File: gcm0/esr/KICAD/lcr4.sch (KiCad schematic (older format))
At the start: 107 parts, among them J1 Conn_Coaxial, J2 Conn_Coaxial, J3 Conn_Coaxial, J4 Conn_Coaxial, SW1 SW_Push, SW2 SW_Push, U1 NE5532, U2 CD4053B, U3 TL084, U4 LM7805_TO220, U5 LM2596S-5, U6 LM1117-3.3, U7 74HC595, U8 STM32F030F4P6, Y1 8M

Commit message: esr电路改错
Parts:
- removed J1, J2, J3, J4: Conn_Coaxial, symbol Connector:Conn_Coaxial
- added D15, D16: 1N4007, Diode_THT:D_DO-41_SOD81_P10.16mm_Horizontal, symbol Diode:1N4007
- added J1, J2, J3, J4: Conn_01x01_Male, Connector_PinHeader_2.54mm:PinHeader_1x01_P2.54mm_Vertical, symbol Connector:Conn_01x01_Male
- added K1, K2: DIPxx-1Axx-11x, Relay_THT:Relay_SPDT_Finder_36.11, symbol Relay:DIPxx-1Axx-11x
- added Q1, Q2: BC547, Package_TO_SOT_THT:TO-92_Inline, symbol Transistor_BJT:BC547
- added R39: 100, Resistor_THT:R_Axial_DIN0204_L3.6mm_D1.6mm_P2.54mm_Vertical, symbol Device:R
- added R40: 1, Resistor_THT:R_Axial_DIN0204_L3.6mm_D1.6mm_P2.54mm_Vertical, symbol Device:R
- added R41, R42: R, Resistor_THT:R_Axial_DIN0204_L3.6mm_D1.6mm_P2.54mm_Vertical, symbol Device:R
- C1, C2, C4: footprint (none) -> Capacitor_THT:C_Rect_L11.0mm_W4.2mm_P10.00mm_MKT
- C10, C11, C12, C13, C14, C15, C16, C17, C18, C19, C20, C21, C22, C23, C24, C25, C26, C27, C28, C29, C3, C31, C32, C33, C34, C35, C36, C37, C5, C6, C7, C8, C9: footprint (none) -> Capacitor_SMD:C_0805_2012Metric_Pad1.18x1.45mm_HandSolder
- C30: value C -> 104; footprint (none) -> Capacitor_SMD:C_0805_2012Metric_Pad1.18x1.45mm_HandSolder
- L1: footprint (none) -> Inductor_THT:L_Radial_D8.7mm_P5.00mm_Fastron_07HCP
- R1: value 100 -> 10K; footprint (none) -> Resistor_THT:R_Axial_DIN0204_L3.6mm_D1.6mm_P2.54mm_Vertical
- R10, R11, R12, R13, R14, R15, R16, R17, R18, R19, R2, R20, R21, R22, R23, R24, R25, R26, R3, R32, R33, R34, R35, R36, R37, R38, R4, R5, R6, R7, R8, R9: footprint (none) -> Resistor_THT:R_Axial_DIN0204_L3.6mm_D1.6mm_P2.54mm_Vertical
- R27, R28, R29: value R -> 10K; footprint (none) -> Resistor_THT:R_Axial_DIN0204_L3.6mm_D1.6mm_P2.54mm_Vertical
- R30: value R -> 1.5K; footprint (none) -> Resistor_THT:R_Axial_DIN0204_L3.6mm_D1.6mm_P2.54mm_Vertical
- R31: value R -> 1K; footprint (none) -> Resistor_THT:R_Axial_DIN0204_L3.6mm_D1.6mm_P2.54mm_Vertical
- SW1, SW2: footprint (none) -> Button_Switch_THT:SW_Tactile_SPST_Angled_PTS645Vx83-2LFS
- TR1: footprint (none) -> Transformer_THT:Transformer_Toroid_Horizontal_D10.5mm_Amidon-T37
- U1: footprint (none) -> Package_DIP:DIP-8_W7.62mm
- U2, U7: footprint (none) -> Package_DIP:DIP-16_W7.62mm
- U3: footprint (none) -> Package_DIP:DIP-14_W7.62mm
- U6: footprint (none) -> Package_TO_SOT_SMD:SOT-223-3_TabPin2
- Y1: footprint (none) -> Crystal:Crystal_HC49-U_Vertical
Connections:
- net +5V: now also D15.1 (K), D16.1 (K), K1.7, K1.8, K2.7, K2.8
- net GND: now also Q1.3 (E), Q2.3 (E)
- net at R3.2: now also J3.1 (Pin_1)
- net at TR1.1: now also J4.1 (Pin_1)
- net at R1.2: now also J1.1 (Pin_1), K1.2, K2.2
- net at R2.2: now also J2.1 (Pin_1)
- net at R1.1, R9.2, TR1.2: now also R39.1, R40.1
- net PA6_1_R: now reaches U8.12 (PA6)
- net PA6_1_R: now also R41.1
- net PA9_100_R: now reaches U8.17 (PA9)
- net PA9_100_R: now also R42.1
- new net: D15.2 (A), K1.1, K1.14, Q1.1 (C)
- new net: K1.6, R39.2
- new net: D16.2 (A), K2.1, K2.14, Q2.1 (C)
- new net: K2.6, R40.2
- new net: Q1.2 (B), R42.2
- new net: Q2.2 (B), R41.2
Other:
- moved on the sheet: C1, D3, D6, R2, R5

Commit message: 修改电路
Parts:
- R41: value R -> 1K
- R42: value R -> 1k
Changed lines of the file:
@@
 P 4400 5350
 F 0 "R41" V 4193 5350 50  0000 C CNN
-F 1 "R" V 4284 5350 50  0000 C CNN
+F 1 "1K" V 4284 5350 50  0000 C CNN
 F 2 "Resistor_THT:R_Axial_DIN0204_L3.6mm_D1.6mm_P2.54mm_Vertical" V 4330 5350 50  0001 C CNN
 F 3 "~" H 4400 5350 50  0001 C CNN
@@
 P 4400 5650
 F 0 "R42" V 4193 5650 50  0000 C CNN
-F 1 "R" V 4284 5650 50  0000 C CNN
+F 1 "1k" V 4284 5650 50  0000 C CNN
 F 2 "Resistor_THT:R_Axial_DIN0204_L3.6mm_D1.6mm_P2.54mm_Vertical" V 4330 5650 50  0001 C CNN
 F 3 "~" H 4400 5650 50  0001 C CNN

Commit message: ..
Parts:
- removed D15, D16: 1N4007, Diode_THT:D_DO-41_SOD81_P10.16mm_Horizontal, symbol Diode:1N4007
- removed K1, K2: DIPxx-1Axx-11x, Relay_THT:Relay_SPDT_Finder_36.11, symbol Relay:DIPxx-1Axx-11x
- removed Q1, Q2: BC547, Package_TO_SOT_THT:TO-92_Inline, symbol Transistor_BJT:BC547
- removed R1: 10K, Resistor_THT:R_Axial_DIN0204_L3.6mm_D1.6mm_P2.54mm_Vertical, symbol Device:R
- removed R39: 100, Resistor_THT:R_Axial_DIN0204_L3.6mm_D1.6mm_P2.54mm_Vertical, symbol Device:R
- removed R40: 1, Resistor_THT:R_Axial_DIN0204_L3.6mm_D1.6mm_P2.54mm_Vertical, symbol Device:R
- removed R41: 1K, Resistor_THT:R_Axial_DIN0204_L3.6mm_D1.6mm_P2.54mm_Vertical, symbol Device:R
- removed R42: 1k, Resistor_THT:R_Axial_DIN0204_L3.6mm_D1.6mm_P2.54mm_Vertical, symbol Device:R
- added R?: 100, symbol Device:R
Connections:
- net at R9.2, TR1.2: now also R?.1
- net at J1.1 (Pin_1): now also R?.2
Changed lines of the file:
@@
 	2050 2600 1650 2600
-$Comp
-L Device:R R1
-U 1 1 62031458
-P 1700 4350
-F 0 "R1" H 1770 4396 50  0000 L CNN
-F 1 "10K" H 1770 4305 50  0000 L CNN
-F 2 "Resistor_THT:R_Axial_DIN0204_L3.6mm_D1.6mm_P2.54mm_Vertical" V 1630 4350 50  0001 C CNN
-F 3 "~" H 1700 4350 50  0001 C CNN
-	1    1700 4350
-	1    0    0    -1
-$EndComp
 $Comp
 L Device:C C3
@@
 	1650 5800 1600 5800
 Wire Wire Line
-	1600 5150 1700 5150
-Wire Wire Line
-	1700 4200 1700 4100
-Wire Wire Line
 	1700 3600 2050 3600
-Wire Wire Line
-	1700 4500 1700 5150
 Wire Wire Line
 	3700 4250 3800 4250
@@
 	9050 3900 9050 4000
 Connection ~ 9050 4000
-$Comp
-L Relay:DIPxx-1Axx-11x K1
-U 1 1 620DB42C
-P 2250 4850
-F 0 "K1" H 2200 4550 50  0000 L CNN
-F 1 "DIPxx-1Axx-11x" H 1700 4400 50  0000 L CNN
-F 2 "Relay_THT:Relay_SPDT_Finder_36.11" H 2600 4800 50  0001 L CNN
-F 3 "https://standexelectronics.com/wp-content/uploads/datasheet_reed_relay_DIP.pdf" H 2250 4850 50  0001 C CNN
-	1    2250 4850
-	1    0    0    -1
-$EndComp
-$Comp
-L Relay:DIPxx-1Axx-11x K2
-U 1 1 620DE9A0
-P 3450 4850
-F 0 "K2" H 3400 5150 50  0000 L CNN
-F 1 "DIPxx-1Axx-11x" H 2950 4500 50  0000 L CNN
-F 2 "Relay_THT:Relay_SPDT_Finder_36.11" H 3800 4800 50  0001 L CNN
-F 3 "https://standexelectronics.com/wp-content/uploads/datasheet_reed_relay_DIP.pdf" H 3450 4850 50  0001 C CNN
-	1    3450 4850
-	1    0    0    -1
-$EndComp
 Wire Wire Line
 	1650 5800 1650 6400
@@
 Wire Wire Line
 	9050 4000 9050 6350
-$Comp
-L Device:R R39
-U 1 1 621A97B2
-P 2050 4350
-F 0 "R39" H 2120 4396 50  0000 L CNN
-F 1 "100" H 2120 4305 50  0000 L CNN
-F 2 "Resistor_THT:R_Axial_DIN0204_L3.6mm_D1.6mm_P2.54mm_Vertical" V 1980 4350 50  0001 C CNN
-F 3 "~" H 2050 4350 50  0001 C CNN
-	1    2050 4350
-	1    0    0    -1
-$EndComp
-$Comp
-L Device:R R40
-U 1 1 621CA5FA
-P 3000 4350
-F 0 "R40" H 3070 4396 50  0000 L CNN
-F 1 "1" H 3070 4305 50  0000 L CNN
-F 2 "Resistor_THT:R_Axial_DIN0204_L3.6mm_D1.6mm_P2.54mm_Vertical" V 2930 4350 50  0001 C CNN
-F 3 "~" H 3000 4350 50  0001 C CNN
-	1    3000 4350
-	1    0    0    -1
-$EndComp
 Wire Wire Line
 	3000 4200 3000 4100
-Wire Wire Line
-	2050 4200 2050 4100
-Connection ~ 2050 4100
-Wire Wire Line
-	2050 4100 1700 4100
 Connection ~ 3000 4100
 Wire Wire Line
-	2050 4100 3000 4100
-Wire Wire Line
-	3000 4500 3000 4550
-Wire Wire Line
-	3000 4550 3250 4550
-Wire Wire Line
-	2050 4500 2050 4550
-Wire Wire Line
-	2050 5150 1700 5150
-Connection ~ 1700 5150
-Wire Wire Line
-	3250 5150 3250 5950
-Wire Wire Line
-	3250 5950 2050 5950
-Wire Wire Line
-	2050 5950 2050 5150
-Connection ~ 2050 5150
-$Comp
-L Transistor_BJT:BC547 Q1
-U 1 1 6238DF6C
-P 2700 5350
-F 0 "Q1" H 2891 5396 50  0000 L CNN
-F 1 "BC547" H 2891 5305 50  0000 L CNN
-F 2 "Package_TO_SOT_THT:TO-92_Inline" H 2900 5275 50  0001 L CIN
-F 3 "https://www.onsemi.com/pub/Collateral/BC550-D.pdf" H 2700 5350 50  0001 L CNN
-	1    2700 5350
-	-1   0    0    -1
-$EndComp
-$Comp
-L Diode:1N4007 D15
-U 1 1 62391AE0
-P 2650 4850
-F 0 "D15" V 2604 4930 50  0000 L CNN
-F 1 "1N4007" V 2695 4930 50  0000 L CNN
-F 2 "Diode_THT:D_DO-41_SOD81_P10.16mm_Horizontal" H 2650 4675 50  0001 C CNN
-F 3 "http://www.vishay.com/docs/88503/1n4001.pdf" H 2650 4850 50  0001 C CNN
-	1    2650 4850
-	0    1    1    0
-$EndComp
-$Comp
-L Diode:1N4007 D16
-U 1 1 62394934
-P 3850 4850
-F 0 "D16" V 3804 4930 50  0000 L CNN
-F 1 "1N4007" V 3895 4930 50  0000 L CNN
-F 2 "Diode_THT:D_DO-41_SOD81_P10.16mm_Horizontal" H 3850 4675 50  0001 C CNN
-F 3 "http://www.vishay.com/docs/88503/1n4001.pdf" H 3850 4850 50  0001 C CNN
-	1    3850 4850
-	0    1    1    0
-$EndComp
-Wire Wire Line
-	3650 4550 3850 4550
-Wire Wire Line
 	3850 4550 3850 4600
-Wire Wire Line
-	2450 4550 2550 4550
-Wire Wire Line
-	2650 4550 2650 4700
-Wire Wire Line
-	2650 5000 2650 5150
-Wire Wire Line
-	2650 5150 2600 5150
-Wire Wire Line
-	3850 5000 3850 5150
-Wire Wire Line
-	3850 5150 3650 5150
-Connection ~ 2600 5150
-Wire Wire Line
-	2600 5150 2450 5150
-$Comp
-L power:GND #PWR025
-U 1 1 6247383D
-P 2600 5550
-F 0 "#PWR025" H 2600 5300 50  0001 C CNN
-F 1 "GND" H 2605 5377 50  0000 C CNN
-F 2 "" H 2600 5550 50  0001 C CNN
-F 3 "" H 2600 5550 50  0001 C CNN
-	1    2600 5550
-	1    0    0    -1
-$EndComp
-$Comp
-L Transistor_BJT:BC547 Q2
-U 1 1 62474772
-P 3950 5350
-F 0 "Q2" H 4141 5396 50  0000 L CNN
-F 1 "BC547" H 4141 5305 50  0000 L CNN
-F 2 "Package_TO_SOT_THT:TO-92_Inline" H 4150 5275 50  0001 L CIN
-F 3 "https://www.onsemi.com/pub/Collateral/BC550-D.pdf" H 3950 5350 50  0001 L CNN
-	1    3950 5350
-	-1   0    0    -1
-$EndComp
-Connection ~ 3850 5150
-$Comp
-L Device:R R41
-U 1 1 6249C881
-P 4400 5350
-F 0 "R41" V 4193 5350 50  0000 C CNN
-F 1 "1K" V 4284 5350 50  0000 C CNN
-F 2 "Resistor_THT:R_Axial_DIN0204_L3.6mm_D1.6mm_P2.54mm_Vertical" V 4330 5350 50  0001 C CNN
-F 3 "~" H 4400 5350 50  0001 C CNN
-	1    4400 5350
-	0    1    1    0
-$EndComp
-$Comp
-L Device:R R42
-U 1 1 6249E143
-P 4400 5650
-F 0 "R42" V 4193 5650 50  0000 C CNN
-F 1 "1k" V 4284 5650 50  0000 C CNN
-F 2 "Resistor_THT:R_Axial_DIN0204_L3.6mm_D1.6mm_P2.54mm_Vertical" V 4330 5650 50  0001 C CNN
-F 3 "~" H 4400 5650 50  0001 C CNN
-	1    4400 5650
-	0    1    1    0
-$EndComp
-$Comp
-L power:GND #PWR026
-U 1 1 624A01EE
-P 3850 5550
-F 0 "#PWR026" H 3850 5300 50  0001 C CNN
-F 1 "GND" H 3855 5377 50  0000 C CNN
-F 2 "" H 3850 5550 50  0001 C CNN
-F 3 "" H 3850 5550 50  0001 C CNN
-	1    3850 5550
-	1    0    0    -1
-$EndComp
-$Comp
-L power:+5V #PWR024
-U 1 1 624A2D0C
-P 2550 4550
-F 0 "#PWR024" H 2550 4400 50  0001 C CNN
-F 1 "+5V" H 2565 4723 50  0000 C CNN
-F 2 "" H 2550 4550 50  0001 C CNN
-F 3 "" H 2550 4550 50  0001 C CNN
-	1    2550 4550
-	1    0    0    -1
-$EndComp
-Connection ~ 2550 4550
-Wire Wire Line
-	2550 4550 2650 4550
 $Comp
 L power:+5V #PWR027
@@
 Wire Wire Line
 	3850 4600 3850 4700
-Wire Wire Line
-	4250 5350 4150 5350
-Wire Wire Line
-	4250 5650 4200 5650
-Wire Wire Line
-	4200 5650 4200 5800
-Wire Wire Line
-	4200 5800 2900 5800
-Wire Wire Line
-	2900 5800 2900 5350
 Text Label 14450 8650 0    50   ~ 0
 PA6_1_R
@@
 Wire Wire Line
 	14450 8850 14300 8850
-Text Label 4700 5350 0    50   ~ 0
-PA6_1_R
-Text Label 4700 5650 0    50   ~ 0
-PA9_100_R
-Wire Wire Line
-	4550 5350 4700 5350
-Wire Wire Line
-	4550 5650 4700 5650
 $Comp
 L Connector:Conn_01x01_Male J3
@@
 Wire Notes Line
 	1500 1950 800  1950
+$Comp
+L Device:R R?
+U 1 1 627C1613
+P 1700 4550
+F 0 "R?" H 1770 4596 50  0000 L CNN
+F 1 "100" H 1770 4505 50  0000 L CNN
+F 2 "" V 1630 4550 50  0001 C CNN
+F 3 "~" H 1700 4550 50  0001 C CNN
+	1    1700 4550
+	1    0    0    -1
+$EndComp
+Wire Wire Line
+	1700 4100 1700 4400
+Wire Wire Line
+	1700 4700 1700 5150
+Wire Wire Line
+	1700 5150 1600 5150
+Wire Wire Line
+	1700 4100 3000 4100
 $EndSCHEMATC

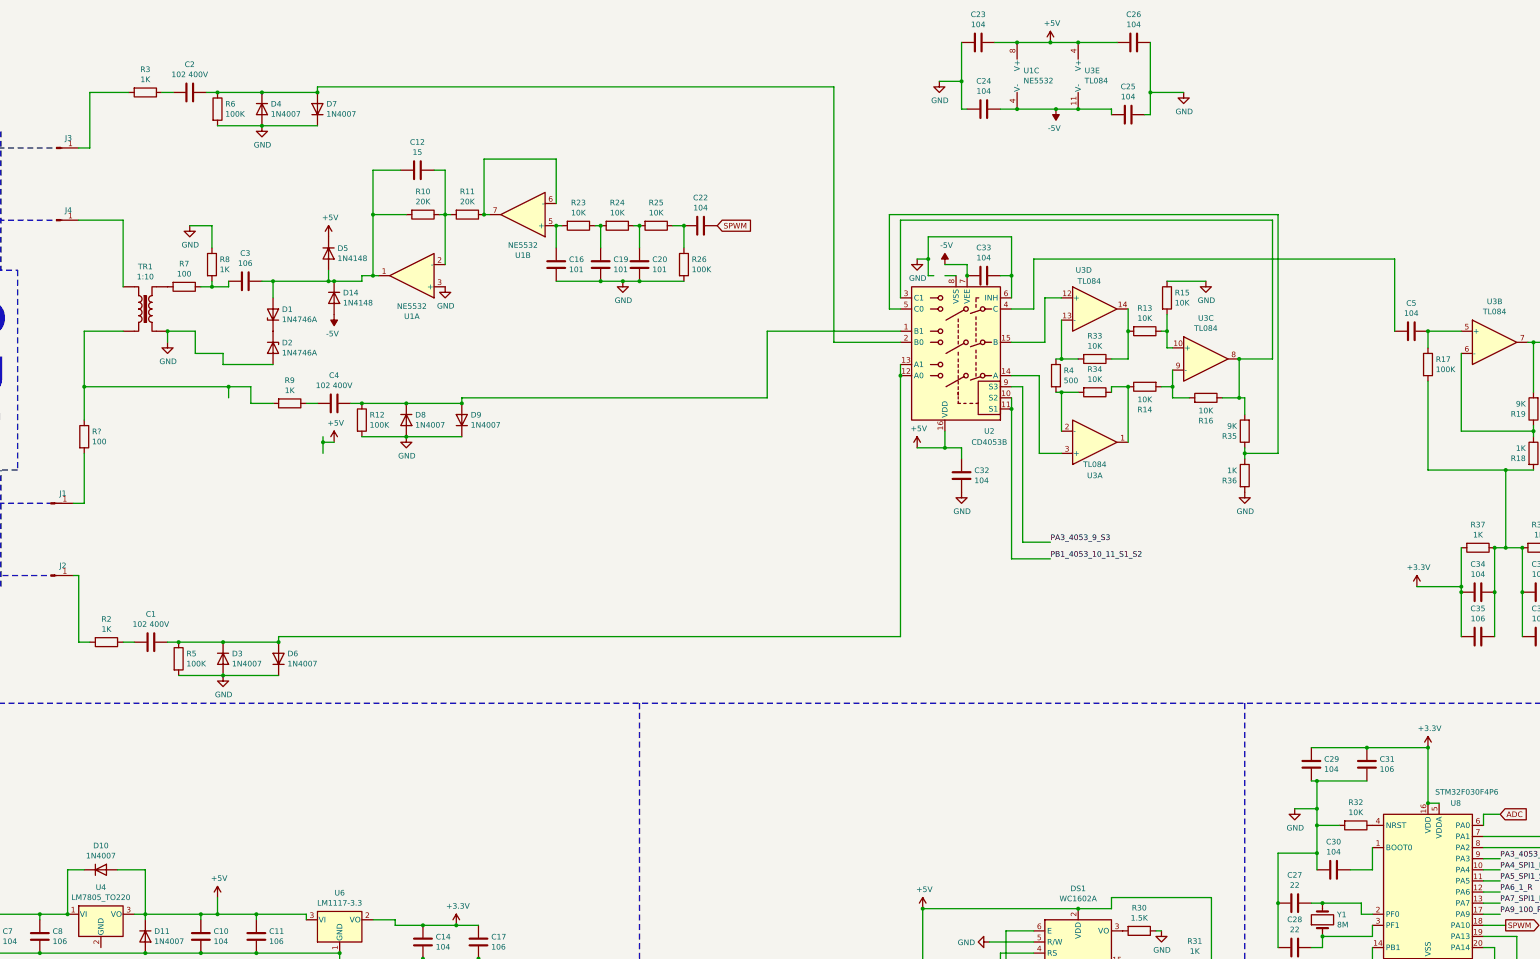
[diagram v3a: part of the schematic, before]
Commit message: 电路改错
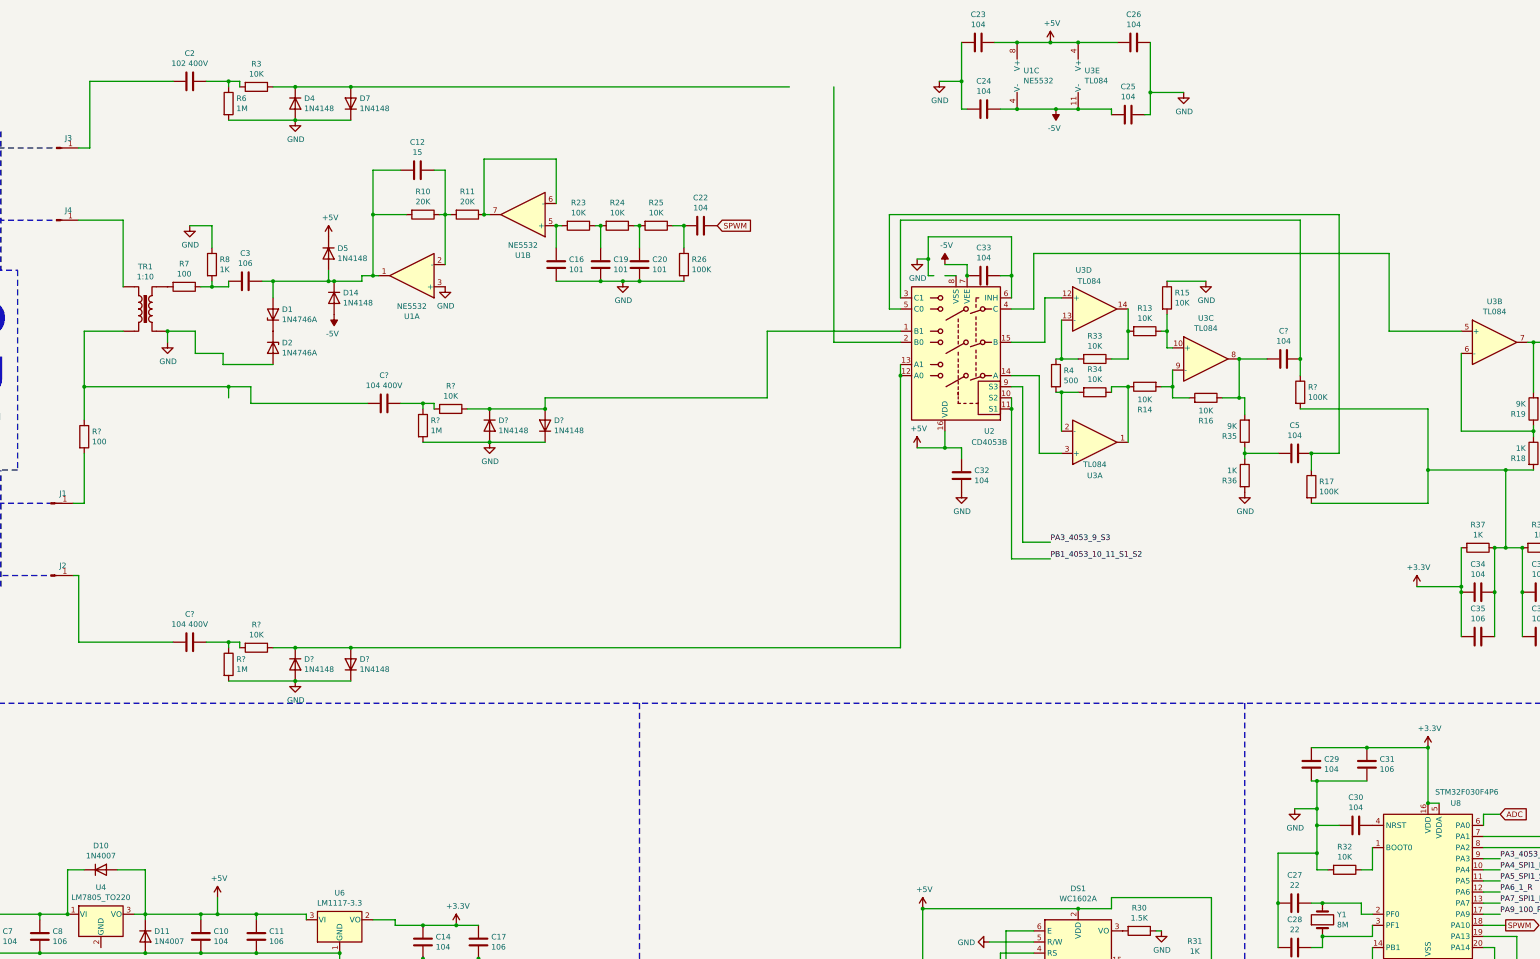
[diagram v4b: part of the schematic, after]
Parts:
- removed C1, C4: 102 400V, Capacitor_THT:C_Rect_L11.0mm_W4.2mm_P10.00mm_MKT, symbol Device:C
- removed D3, D6, D8, D9: 1N4007, Diode_THT:D_DO-41_SOD81_P10.16mm_Horizontal, symbol Diode:1N4007
- removed R12, R5: 100K, Resistor_THT:R_Axial_DIN0204_L3.6mm_D1.6mm_P2.54mm_Vertical, symbol Device:R
- removed R2, R9: 1K, Resistor_THT:R_Axial_DIN0204_L3.6mm_D1.6mm_P2.54mm_Vertical, symbol Device:R
- added C? (x2): 104 400V, Capacitor_THT:C_Rect_L11.0mm_W4.2mm_P10.00mm_MKT, symbol Device:C
- added C?: 104, Capacitor_SMD:C_0805_2012Metric_Pad1.18x1.45mm_HandSolder, symbol Device:C
- added D? (x4): 1N4148, Diode_THT:D_DO-41_SOD81_P10.16mm_Horizontal, symbol Diode:1N4007
- added R? (x2): 10K, Resistor_THT:R_Axial_DIN0204_L3.6mm_D1.6mm_P2.54mm_Vertical, symbol Device:R
- added R? (x2): 1M, Resistor_THT:R_Axial_DIN0204_L3.6mm_D1.6mm_P2.54mm_Vertical, symbol Device:R
- added R?: 100K, Resistor_THT:R_Axial_DIN0204_L3.6mm_D1.6mm_P2.54mm_Vertical, symbol Device:R
- D4, D7: value 1N4007 -> 1N4148
- R3: value 1K -> 10K
- R6: value 100K -> 1M
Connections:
- net GND: now also D?.1 (K), D?.1 (K), D?.2 (A), D?.2 (A), R?.2, R?.2
- net at R?.1, TR1.2: now also C?.2
- net at U2.1 (B1): now also D?.1 (K), D?.2 (A), R?.1
- net at U2.12 (A0), U2.13 (A1): now also D?.1 (K), D?.2 (A), R?.1
- net at R16.1, R35.2, U3.8: now also C?.2; no longer U2.3 (C1)
- net at U2.4 (C): now also U3.5 (+); no longer C5.2
- net at R35.1, R36.1: now also C5.2; no longer U2.5 (C0)
- net at R3.1: now also D4.1 (K), D7.2 (A); no longer C2.2
- net at R3.2: now also C2.1, R6.1; no longer J3.1 (Pin_1)
- net at C5.1, R17.1: now also U2.5 (C0); no longer U3.5 (+)
- net at J2.1 (Pin_1): now also C?.2
- net at C34.1, C35.1, C36.2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: now also R?.2
- net at U8.1 (BOOT0): now also R32.1; no longer C30.1
- net at U8.4 (NRST): now also C30.1; no longer R32.1
- new net: C?.1, R?.1, U2.3 (C1)
- new net: C2.2, J3.1 (Pin_1)
- new net: C?.1, R?.1, R?.2 (x2)
- now unconnected: U2.2 (B0)
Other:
- moved on the sheet: C2, C30, C5, D4, D7, R17, R3, R32, R6
